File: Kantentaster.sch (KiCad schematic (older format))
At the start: 20 parts, among them P1 Anschluss Kantentaster, P3 Anschluss_USB_CNC, U1 LM324

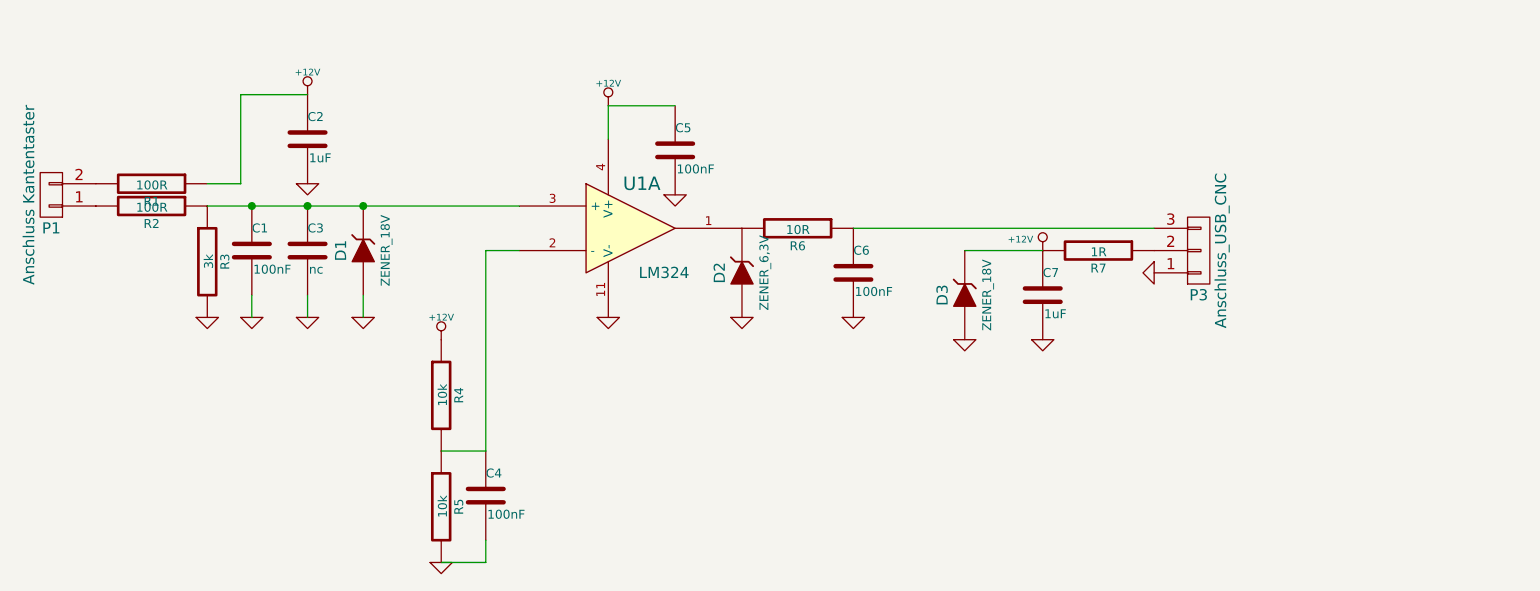
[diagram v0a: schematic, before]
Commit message: anpassungen am schaltplan und layout
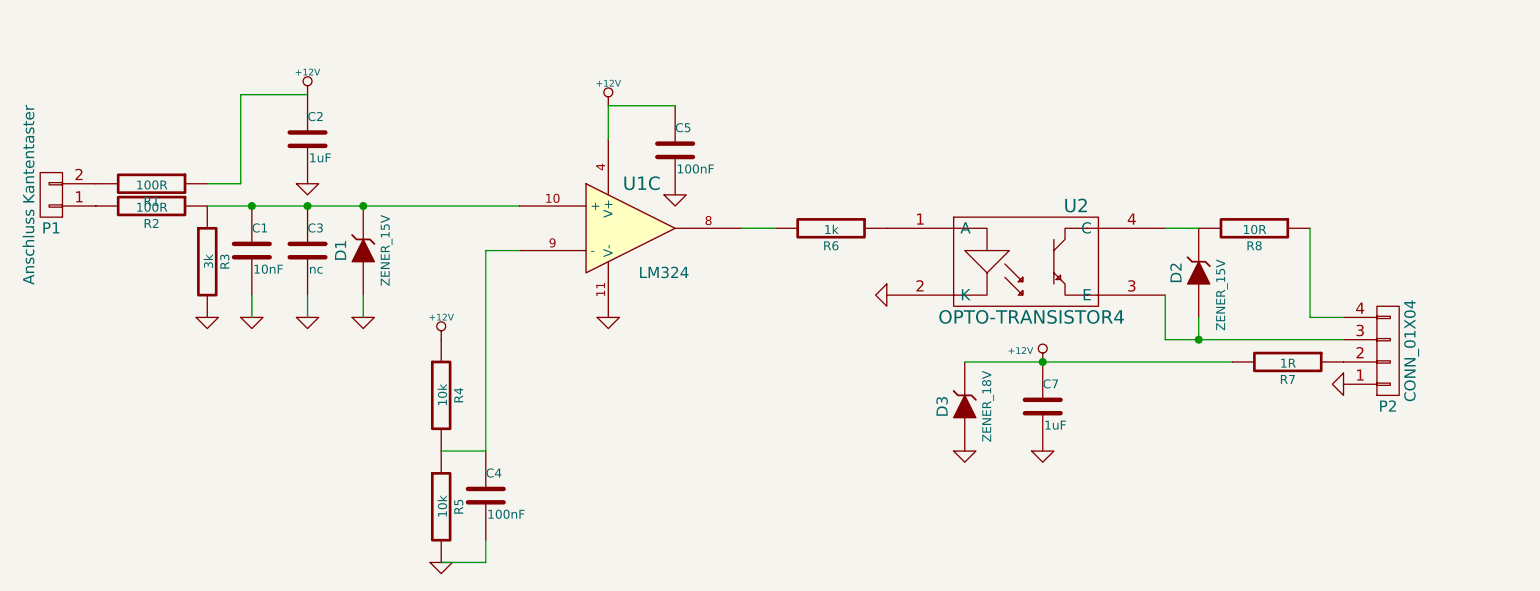
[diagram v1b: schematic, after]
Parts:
- removed C6: 100nF, Capacitors_SMD:C_0603, symbol C
- removed P3: Anschluss_USB_CNC, symbol CONN_01X03
- removed U1: LM324, SMD_Packages:SOIC-14_N, symbol LM324
- added P2: CONN_01X04, symbol CONN_01X04
- added R8: 10R, symbol R
- added U1: LM324, symbol LM324
- added U2: OPTO-TRANSISTOR4, symbol OPTO-TRANSISTOR4
- C1: value 100nF -> 10nF
- D1: value ZENER_18V -> ZENER_15V
- D2: value ZENER_6,3V -> ZENER_15V; footprint Diodes_SMD:Diode-SMA_Handsoldering -> (none)
- R6: value 10R -> 1k
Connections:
- net +12V: now also U1.4 (V+)
- net GND: now also P2.1 (P1), U1.11 (V-), U2.2 (K); no longer D2.1 (A)
- net at C1.1, C3.1, D1.2 (K)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: now also U1.10 (+)
- net at R6.2: now also U1.8; no longer D2.2 (K)
- net at C4.1, R4.2, R5.1: now also U1.9 (-)
- net at R6.1: now also U2.1 (A)
- net at R7.1: now also P2.2 (P2)
- new net: D2.1 (A), P2.3 (P3), U2.3 (E)
- new net: P2.4 (P4), R8.1
- new net: D2.2 (K), R8.2, U2.4 (C)
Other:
- moved on the sheet: C7, D3, R6, R7

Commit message: Mitkopplung hinzugefügt
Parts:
- added R9: 200k, Resistors_SMD:R_0805, symbol R
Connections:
- net at C1.1, C3.1, D1.2 (K)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: now also R9.2
- net at R6.2, U1.8: now also R9.1
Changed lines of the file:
@@
 $EndComp
 $Comp
-L GND #PWR1
+L GND #PWR01
 U 1 1 54ECF78A
 P 2000 2350
-F 0 "#PWR1" H 2000 2350 30  0001 C CNN
+F 0 "#PWR01" H 2000 2350 30  0001 C CNN
 F 1 "GND" H 2000 2280 30  0001 C CNN
 F 2 "" H 2000 2350 60  0000 C CNN
@@
 $EndComp
 $Comp
-L GND #PWR2
+L GND #PWR02
 U 1 1 54ECF7A2
 P 2200 2350
-F 0 "#PWR2" H 2200 2350 30  0001 C CNN
+F 0 "#PWR02" H 2200 2350 30  0001 C CNN
 F 1 "GND" H 2200 2280 30  0001 C CNN
 F 2 "" H 2200 2350 60  0000 C CNN
@@
 $EndComp
 $Comp
-L GND #PWR5
+L GND #PWR03
 U 1 1 54ECF7B3
 P 2450 2350
-F 0 "#PWR5" H 2450 2350 30  0001 C CNN
+F 0 "#PWR03" H 2450 2350 30  0001 C CNN
 F 1 "GND" H 2450 2280 30  0001 C CNN
 F 2 "" H 2450 2350 60  0000 C CNN
@@
 $EndComp
 $Comp
-L GND #PWR6
+L GND #PWR04
 U 1 1 54ECF7C4
 P 2700 2350
-F 0 "#PWR6" H 2700 2350 30  0001 C CNN
+F 0 "#PWR04" H 2700 2350 30  0001 C CNN
 F 1 "GND" H 2700 2280 30  0001 C CNN
 F 2 "" H 2700 2350 60  0000 C CNN
@@
 $EndComp
 $Comp
-L +12V #PWR3
+L +12V #PWR05
 U 1 1 54ECF89F
 P 2450 1350
-F 0 "#PWR3" H 2450 1300 20  0001 C CNN
+F 0 "#PWR05" H 2450 1300 20  0001 C CNN
 F 1 "+12V" H 2450 1450 30  0000 C CNN
 F 2 "" H 2450 1350 60  0000 C CNN
@@
 $EndComp
 $Comp
-L GND #PWR4
+L GND #PWR06
 U 1 1 54ECFA9A
 P 2450 1750
-F 0 "#PWR4" H 2450 1750 30  0001 C CNN
+F 0 "#PWR06" H 2450 1750 30  0001 C CNN
 F 1 "GND" H 2450 1680 30  0001 C CNN
 F 2 "" H 2450 1750 60  0000 C CNN
@@
 Connection ~ 2700 1850
 $Comp
-L GND #PWR10
+L GND #PWR07
 U 1 1 54ECFC8D
 P 3800 2350
-F 0 "#PWR10" H 3800 2350 30  0001 C CNN
+F 0 "#PWR07" H 3800 2350 30  0001 C CNN
 F 1 "GND" H 3800 2280 30  0001 C CNN
 F 2 "" H 3800 2350 60  0000 C CNN
@@
 $EndComp
 $Comp
-L +12V #PWR9
+L +12V #PWR08
 U 1 1 54ECFCB0
 P 3800 1400
-F 0 "#PWR9" H 3800 1350 20  0001 C CNN
+F 0 "#PWR08" H 3800 1350 20  0001 C CNN
 F 1 "+12V" H 3800 1500 30  0000 C CNN
 F 2 "" H 3800 1400 60  0000 C CNN
@@
 	3050 2950 3250 2950
 $Comp
-L +12V #PWR7
+L +12V #PWR09
 U 1 1 54ECFF88
 P 3050 2450
-F 0 "#PWR7" H 3050 2400 20  0001 C CNN
+F 0 "#PWR09" H 3050 2400 20  0001 C CNN
 F 1 "+12V" H 3050 2550 30  0000 C CNN
 F 2 "" H 3050 2450 60  0000 C CNN
@@
 $EndComp
 $Comp
-L GND #PWR8
+L GND #PWR010
 U 1 1 54ECFFC6
 P 3050 3450
-F 0 "#PWR8" H 3050 3450 30  0001 C CNN
+F 0 "#PWR010" H 3050 3450 30  0001 C CNN
 F 1 "GND" H 3050 3380 30  0001 C CNN
 F 2 "" H 3050 3450 60  0000 C CNN
@@
 $EndComp
 $Comp
-L GND #PWR16
+L GND #PWR011
 U 1 1 54ED05FF
 P 7100 2650
-F 0 "#PWR16" H 7100 2650 30  0001 C CNN
+F 0 "#PWR011" H 7100 2650 30  0001 C CNN
 F 1 "GND" H 7100 2580 30  0001 C CNN
 F 2 "" H 7100 2650 60  0000 C CNN
@@
 $EndComp
 $Comp
-L +12V #PWR14
+L +12V #PWR012
 U 1 1 54ED080B
 P 5750 2550
-F 0 "#PWR14" H 5750 2500 20  0001 C CNN
+F 0 "#PWR012" H 5750 2500 20  0001 C CNN
 F 1 "+12V" H 5650 2600 30  0000 C CNN
 F 2 "" H 5750 2550 60  0000 C CNN
@@
 $EndComp
 $Comp
-L GND #PWR15
+L GND #PWR013
 U 1 1 54ED0C07
 P 5750 2950
-F 0 "#PWR15" H 5750 2950 30  0001 C CNN
+F 0 "#PWR013" H 5750 2950 30  0001 C CNN
 F 1 "GND" H 5750 2880 30  0001 C CNN
 F 2 "" H 5750 2950 60  0000 C CNN
@@
 $EndComp
 $Comp
-L GND #PWR13
+L GND #PWR014
 U 1 1 54ED1229
 P 5400 2950
-F 0 "#PWR13" H 5400 2950 30  0001 C CNN
+F 0 "#PWR014" H 5400 2950 30  0001 C CNN
 F 1 "GND" H 5400 2880 30  0001 C CNN
 F 2 "" H 5400 2950 60  0000 C CNN
@@
 	3800 1400 4100 1400
 $Comp
-L GND #PWR11
+L GND #PWR015
 U 1 1 54ED197C
 P 4100 1800
-F 0 "#PWR11" H 4100 1800 30  0001 C CNN
+F 0 "#PWR015" H 4100 1800 30  0001 C CNN
 F 1 "GND" H 4100 1730 30  0001 C CNN
 F 2 "" H 4100 1800 60  0000 C CNN
@@
 	4400 1950 4550 1950
 $Comp
-L GND #PWR12
+L GND #PWR016
 U 1 1 54F1DAD4
 P 5050 2250
-F 0 "#PWR12" H 5050 2250 30  0001 C CNN
+F 0 "#PWR016" H 5050 2250 30  0001 C CNN
 F 1 "GND" H 5050 2180 30  0001 C CNN
 F 2 "" H 5050 2250 60  0000 C CNN
@@
 	1    0    0    -1
 $EndComp
+$Comp
+L R R9
+U 1 1 54F25C8A
+P 3800 1050
+F 0 "R9" V 3880 1050 40  0000 C CNN
+F 1 "200k" V 3807 1051 40  0000 C CNN
+F 2 "Resistors_SMD:R_0805" V 3730 1050 30  0001 C CNN
+F 3 "" H 3800 1050 30  0000 C CNN
+	1    3800 1050
+	0    1    1    0
+$EndComp
+Wire Wire Line
+	3550 1050 3400 1050
+Wire Wire Line
+	3400 1050 3400 1850
+Wire Wire Line
+	4050 1050 4400 1050
+Wire Wire Line
+	4400 1050 4400 1950
 $EndSCHEMATC

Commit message: finale Version
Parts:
- added C6: 10nF, Capacitors_SMD:C_0603, symbol C
- D2: footprint (none) -> Diodes_SMD:Diode-SMA_Handsoldering
- P1: footprint (none) -> Pin_Headers:Pin_Header_Angled_1x02
- P2: footprint (none) -> Pin_Headers:Pin_Header_Angled_1x04
- R8: footprint (none) -> Resistors_SMD:R_0805
- U1: footprint (none) -> SMD_Packages:SOIC-14_N
- U2: footprint (none) -> toni:SO-4
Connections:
- net GND: now also C6.2
- net at R6.1, U2.1 (A): now also C6.1
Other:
- moved on the sheet: C7, D2, D3, P2, R7, R8, U2
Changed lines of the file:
@@
 L GND #PWR011
 U 1 1 54ED05FF
-P 7100 2650
-F 0 "#PWR011" H 7100 2650 30  0001 C CNN
-F 1 "GND" H 7100 2580 30  0001 C CNN
-F 2 "" H 7100 2650 60  0000 C CNN
-F 3 "" H 7100 2650 60  0000 C CNN
-	1    7100 2650
+P 7550 2650
+F 0 "#PWR011" H 7550 2650 30  0001 C CNN
+F 1 "GND" H 7550 2580 30  0001 C CNN
+F 2 "" H 7550 2650 60  0000 C CNN
+F 3 "" H 7550 2650 60  0000 C CNN
+	1    7550 2650
 	0    1    1    0
 $EndComp
@@
 L +12V #PWR012
 U 1 1 54ED080B
-P 5750 2550
-F 0 "#PWR012" H 5750 2500 20  0001 C CNN
-F 1 "+12V" H 5650 2600 30  0000 C CNN
-F 2 "" H 5750 2550 60  0000 C CNN
-F 3 "" H 5750 2550 60  0000 C CNN
-	1    5750 2550
+P 6200 2550
+F 0 "#PWR012" H 6200 2500 20  0001 C CNN
+F 1 "+12V" H 6100 2600 30  0000 C CNN
+F 2 "" H 6200 2550 60  0000 C CNN
+F 3 "" H 6200 2550 60  0000 C CNN
+	1    6200 2550
 	1    0    0    -1
 $EndComp
@@
 L R R7
 U 1 1 54ED0ABC
-P 6850 2550
-F 0 "R7" V 6930 2550 40  0000 C CNN
-F 1 "1R" V 6857 2551 40  0000 C CNN
-F 2 "Resistors_SMD:R_0805" V 6780 2550 30  0001 C CNN
-F 3 "" H 6850 2550 30  0000 C CNN
-	1    6850 2550
+P 7300 2550
+F 0 "R7" V 7380 2550 40  0000 C CNN
+F 1 "1R" V 7307 2551 40  0000 C CNN
+F 2 "Resistors_SMD:R_0805" V 7230 2550 30  0001 C CNN
+F 3 "" H 7300 2550 30  0000 C CNN
+	1    7300 2550
 	0    1    1    0
 $EndComp
@@
 L C C7
 U 1 1 54ED0B4D
-P 5750 2750
-F 0 "C7" H 5750 2850 40  0000 L CNN
-F 1 "1uF" H 5756 2665 40  0000 L CNN
-F 2 "Capacitors_SMD:C_0805" H 5788 2600 30  0001 C CNN
-F 3 "" H 5750 2750 60  0000 C CNN
-	1    5750 2750
+P 6200 2750
+F 0 "C7" H 6200 2850 40  0000 L CNN
+F 1 "1uF" H 6206 2665 40  0000 L CNN
+F 2 "Capacitors_SMD:C_0805" H 6238 2600 30  0001 C CNN
+F 3 "" H 6200 2750 60  0000 C CNN
+	1    6200 2750
 	1    0    0    -1
 $EndComp
@@
 L GND #PWR013
 U 1 1 54ED0C07
-P 5750 2950
-F 0 "#PWR013" H 5750 2950 30  0001 C CNN
-F 1 "GND" H 5750 2880 30  0001 C CNN
-F 2 "" H 5750 2950 60  0000 C CNN
-F 3 "" H 5750 2950 60  0000 C CNN
-	1    5750 2950
+P 6200 2950
+F 0 "#PWR013" H 6200 2950 30  0001 C CNN
+F 1 "GND" H 6200 2880 30  0001 C CNN
+F 2 "" H 6200 2950 60  0000 C CNN
+F 3 "" H 6200 2950 60  0000 C CNN
+	1    6200 2950
 	1    0    0    -1
 $EndComp
@@
 L ZENER D3
 U 1 1 54ED0D5B
-P 5400 2750
-F 0 "D3" H 5400 2850 50  0000 C CNN
-F 1 "ZENER_18V" H 5400 2650 40  0000 C CNN
-F 2 "Diodes_SMD:Diode-SMB_Handsoldering" H 5400 2750 60  0001 C CNN
-F 3 "" H 5400 2750 60  0000 C CNN
-	1    5400 2750
+P 5850 2750
+F 0 "D3" H 5850 2850 50  0000 C CNN
+F 1 "ZENER_18V" H 5850 2650 40  0000 C CNN
+F 2 "Diodes_SMD:Diode-SMB_Handsoldering" H 5850 2750 60  0001 C CNN
+F 3 "" H 5850 2750 60  0000 C CNN
+	1    5850 2750
 	0    -1   -1   0
 $EndComp
@@
 L GND #PWR014
 U 1 1 54ED1229
-P 5400 2950
-F 0 "#PWR014" H 5400 2950 30  0001 C CNN
-F 1 "GND" H 5400 2880 30  0001 C CNN
-F 2 "" H 5400 2950 60  0000 C CNN
-F 3 "" H 5400 2950 60  0000 C CNN
-	1    5400 2950
-	1    0    0    -1
-$EndComp
-Wire Wire Line
-	5400 2550 6600 2550
+P 5850 2950
+F 0 "#PWR014" H 5850 2950 30  0001 C CNN
+F 1 "GND" H 5850 2880 30  0001 C CNN
+F 2 "" H 5850 2950 60  0000 C CNN
+F 3 "" H 5850 2950 60  0000 C CNN
+	1    5850 2950
+	1    0    0    -1
+$EndComp
+Wire Wire Line
+	5850 2550 7050 2550
 $Comp
 L C C5
@@
 F 0 "P1" H 1300 1950 50  0000 C CNN
 F 1 "Anschluss Kantentaster" V 1400 1800 50  0000 C CNN
-F 2 "" H 1300 1800 60  0001 C CNN
+F 2 "Pin_Headers:Pin_Header_Angled_1x02" H 1300 1800 60  0001 C CNN
 F 3 "" H 1300 1800 60  0000 C CNN
 	1    1300 1800
@@
 L CONN_01X04 P2
 U 1 1 54F1D48A
-P 7300 2500
-F 0 "P2" H 7300 2750 50  0000 C CNN
-F 1 "CONN_01X04" V 7400 2500 50  0000 C CNN
-F 2 "" H 7300 2500 60  0000 C CNN
-F 3 "" H 7300 2500 60  0000 C CNN
-	1    7300 2500
+P 7750 2500
+F 0 "P2" H 7750 2750 50  0000 C CNN
+F 1 "CONN_01X04" V 7850 2500 50  0000 C CNN
+F 2 "Pin_Headers:Pin_Header_Angled_1x04" H 7750 2500 60  0001 C CNN
+F 3 "" H 7750 2500 60  0000 C CNN
+	1    7750 2500
 	1    0    0    1
 $EndComp
@@
 L OPTO-TRANSISTOR4 U2
 U 1 1 54F1D78F
-P 5700 2100
-F 0 "U2" H 5900 2350 60  0000 C CNN
-F 1 "OPTO-TRANSISTOR4" H 5700 1850 60  0000 C CNN
-F 2 "" H 5700 2100 60  0000 C CNN
-F 3 "" H 5700 2100 60  0000 C CNN
-	1    5700 2100
-	1    0    0    -1
-$EndComp
-Connection ~ 5750 2550
+P 6150 2100
+F 0 "U2" H 6350 2350 60  0000 C CNN
+F 1 "OPTO-TRANSISTOR4" H 6150 1850 60  0000 C CNN
+F 2 "toni:SO-4" H 6150 2100 60  0001 C CNN
+F 3 "" H 6150 2100 60  0000 C CNN
+	1    6150 2100
+	1    0    0    -1
+$EndComp
+Connection ~ 6200 2550
 Wire Wire Line
 	4400 1950 4550 1950
@@
 L GND #PWR016
 U 1 1 54F1DAD4
-P 5050 2250
-F 0 "#PWR016" H 5050 2250 30  0001 C CNN
-F 1 "GND" H 5050 2180 30  0001 C CNN
-F 2 "" H 5050 2250 60  0000 C CNN
-F 3 "" H 5050 2250 60  0000 C CNN
-	1    5050 2250
-	0    1    1    0
-$EndComp
-Wire Wire Line
-	6300 2250 6300 2450
-Wire Wire Line
-	6300 2450 7100 2450
-Wire Wire Line
-	6300 1950 6450 1950
+P 5500 2250
+F 0 "#PWR016" H 5500 2250 30  0001 C CNN
+F 1 "GND" H 5500 2180 30  0001 C CNN
+F 2 "" H 5500 2250 60  0000 C CNN
+F 3 "" H 5500 2250 60  0000 C CNN
+	1    5500 2250
+	0    1    1    0
+$EndComp
+Wire Wire Line
+	6750 2250 6750 2450
+Wire Wire Line
+	6750 2450 7550 2450
+Wire Wire Line
+	6750 1950 6900 1950
 $Comp
 L ZENER D2
 U 1 1 54F1DF54
-P 6450 2150
-F 0 "D2" H 6450 2250 50  0000 C CNN
-F 1 "ZENER_15V" H 6350 2050 40  0000 C CNN
-F 2 "" H 6450 2150 60  0000 C CNN
-F 3 "" H 6450 2150 60  0000 C CNN
-	1    6450 2150
+P 6900 2150
+F 0 "D2" H 6900 2250 50  0000 C CNN
+F 1 "ZENER_15V" H 6800 2050 40  0000 C CNN
+F 2 "Diodes_SMD:Diode-SMA_Handsoldering" H 6900 2150 60  0001 C CNN
+F 3 "" H 6900 2150 60  0000 C CNN
+	1    6900 2150
 	0    -1   -1   0
 $EndComp
@@
 L R R8
 U 1 1 54F1DFD9
-P 6700 1950
-F 0 "R8" V 6780 1950 40  0000 C CNN
-F 1 "10R" V 6707 1951 40  0000 C CNN
-F 2 "" V 6630 1950 30  0000 C CNN
-F 3 "" H 6700 1950 30  0000 C CNN
-	1    6700 1950
-	0    1    1    0
-$EndComp
-Wire Wire Line
-	6450 2350 6450 2450
-Connection ~ 6450 2450
-Wire Wire Line
-	6950 1950 6950 2350
-Wire Wire Line
-	6950 2350 7100 2350
+P 7150 1950
+F 0 "R8" V 7230 1950 40  0000 C CNN
+F 1 "10R" V 7157 1951 40  0000 C CNN
+F 2 "Resistors_SMD:R_0805" V 7080 1950 30  0001 C CNN
+F 3 "" H 7150 1950 30  0000 C CNN
+	1    7150 1950
+	0    1    1    0
+$EndComp
+Wire Wire Line
+	6900 2350 6900 2450
+Connection ~ 6900 2450
+Wire Wire Line
+	7400 1950 7400 2350
+Wire Wire Line
+	7400 2350 7550 2350
 $Comp
 L LM324 U1
@@
 F 0 "U1" H 3950 2150 60  0000 C CNN
 F 1 "LM324" H 4050 1750 50  0000 C CNN
-F 2 "" H 3900 1950 60  0000 C CNN
+F 2 "SMD_Packages:SOIC-14_N" H 3900 1950 60  0001 C CNN
 F 3 "" H 3900 1950 60  0000 C CNN
 	3    3900 1950
@@
 Wire Wire Line
 	4400 1050 4400 1950
+$Comp
+L C C6
+U 1 1 54F850EE
+P 5050 2150
+F 0 "C6" H 5050 2250 40  0000 L CNN
+F 1 "10nF" H 5056 2065 40  0000 L CNN
+F 2 "Capacitors_SMD:C_0603" H 5088 2000 30  0001 C CNN
+F 3 "" H 5050 2150 60  0000 C CNN
+	1    5050 2150
+	1    0    0    -1
+$EndComp
+Wire Wire Line
+	5050 1950 5500 1950
+$Comp
+L GND #PWR017
+U 1 1 54F8527D
+P 5050 2350
+F 0 "#PWR017" H 5050 2350 30  0001 C CNN
+F 1 "GND" H 5050 2280 30  0001 C CNN
+F 2 "" H 5050 2350 60  0000 C CNN
+F 3 "" H 5050 2350 60  0000 C CNN
+	1    5050 2350
+	1    0    0    -1
+$EndComp
 $EndSCHEMATC

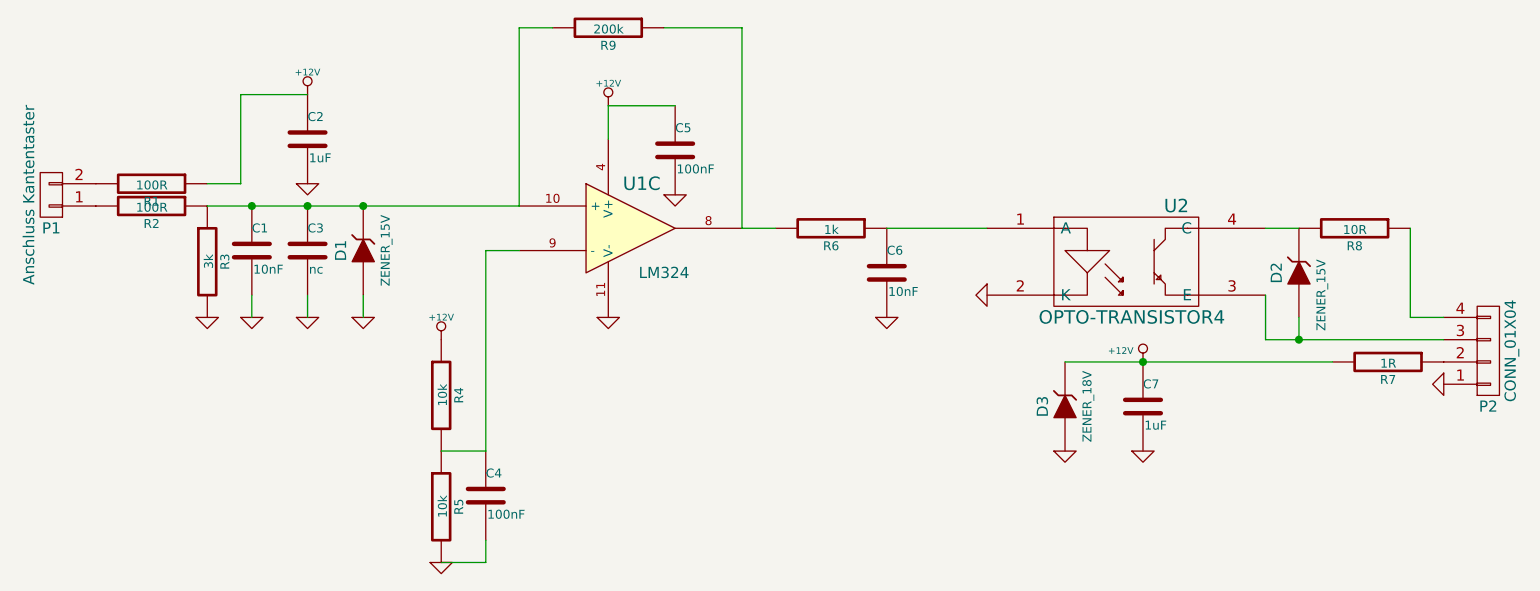
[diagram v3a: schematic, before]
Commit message: Fehler des ersten Prototypen behoben
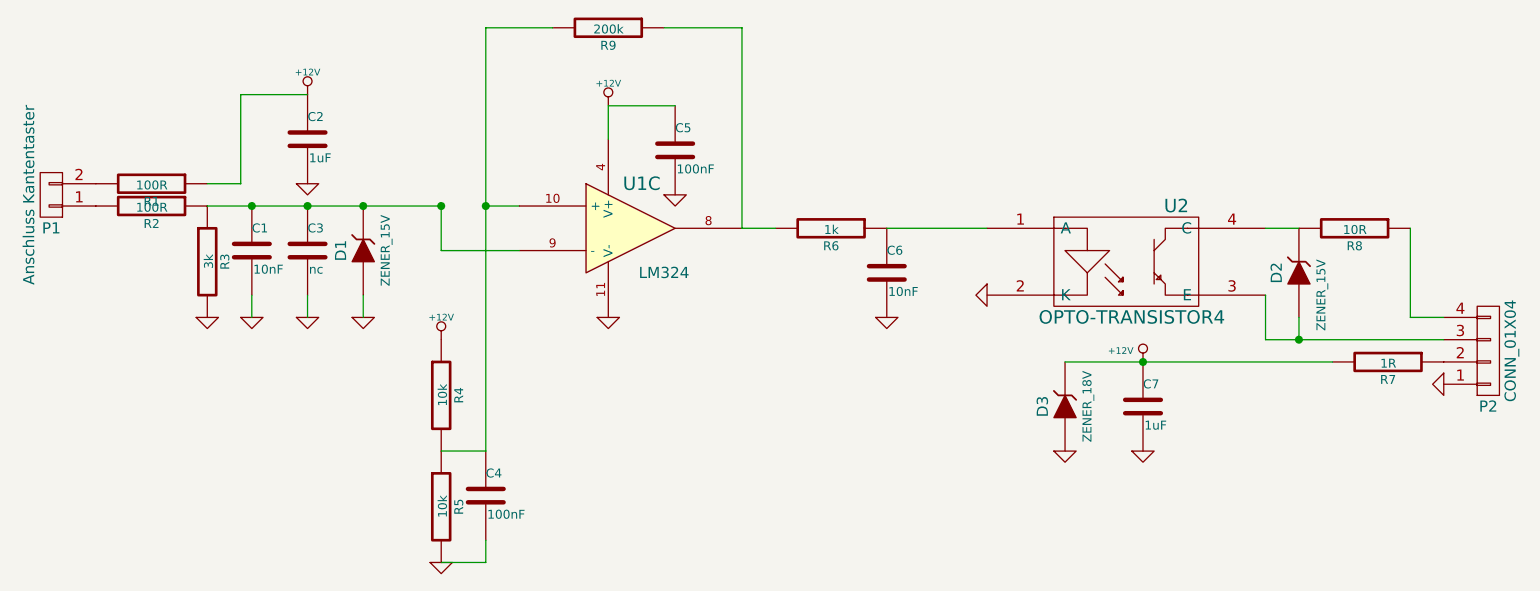
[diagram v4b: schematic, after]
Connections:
- net at C1.1, C3.1, D1.2 (K)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: now also U1.9 (-); no longer R9.2, U1.10 (+)
- net at C4.1, R4.2, R5.1: now also R9.2, U1.10 (+); no longer U1.9 (-)
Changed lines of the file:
@@
 	0    -1   -1   0
 $EndComp
-Wire Wire Line
-	2000 1850 3400 1850
 Connection ~ 2200 1850
 Connection ~ 2450 1850
@@
 	3250 3450 3250 3350
 Wire Wire Line
-	3050 2950 3250 2950
+	3250 2950 3050 2950
 $Comp
 L +12V #PWR09
@@
 	1    0    0    -1
 $EndComp
-Wire Wire Line
-	3250 2950 3250 2050
-Wire Wire Line
-	3250 2050 3400 2050
 $Comp
 L R R6
@@
 $EndComp
 Wire Wire Line
-	3550 1050 3400 1050
-Wire Wire Line
-	3400 1050 3400 1850
-Wire Wire Line
 	4050 1050 4400 1050
 Wire Wire Line
@@
 	1    0    0    -1
 $EndComp
+Wire Wire Line
+	2000 1850 3050 1850
+Connection ~ 3050 1850
+Wire Wire Line
+	3050 2050 3400 2050
+Wire Wire Line
+	3250 1050 3250 2950
+Wire Wire Line
+	3250 1850 3400 1850
+Wire Wire Line
+	3050 1850 3050 2050
+Wire Wire Line
+	3550 1050 3250 1050
+Connection ~ 3250 1850
 $EndSCHEMATC
